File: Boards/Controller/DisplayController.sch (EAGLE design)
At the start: 47 parts, among them J1 USB0001LF, J100 38K8067, J3 AVR_SPI_PRG_62X3_LOCK, Q1 BSS138, U1 MCP1703CB, U100 MCP73831, U101 MAX1797, U2 FT232RQ, U3 ATMEGA328P-MU, U5 MAX1704X, X2 CRYSTAL7A-20.000MAAJ-T

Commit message: Added more xref labels to connections
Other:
- moved on the sheet: J100
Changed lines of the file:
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@@
 <setting verticaltext="up"/>
 </settings>
-<grid distance="0.1" unitdist="inch" unit="inch" style="lines" multiple="1" display="no" altdistance="0.01" altunitdist="inch" altunit="inch"/>
+<grid distance="0.1" unitdist="inch" unit="inch" style="lines" multiple="1" display="no" altdistance="0.05" altunitdist="inch" altunit="inch"/>
 <layers>
 <layer number="1" name="Top" color="4" fill="1" visible="no" active="no"/>
@@
 <part name="P+9" library="supply1" deviceset="VCC" device=""/>
 <part name="P+10" library="supply1" deviceset="VCC" device=""/>
+<part name="GND21" library="SparkFun" deviceset="GND" device=""/>
+<part name="GND27" library="SparkFun" deviceset="GND" device=""/>
+<part name="GND28" library="SparkFun" deviceset="GND" device=""/>
 </parts>
 <sheets>
@@
 <instance part="RN2" gate="A" x="109.22" y="157.48" rot="R270"/>
 <instance part="J2" gate="G$1" x="203.2" y="68.58"/>
-<instance part="J100" gate="G$1" x="160.02" y="93.98"/>
-<instance part="GND20" gate="1" x="172.72" y="86.36"/>
+<instance part="J100" gate="G$1" x="203.2" y="127"/>
+<instance part="GND20" gate="1" x="215.9" y="119.38"/>
 <instance part="J3" gate="G$1" x="200.66" y="93.98" smashed="yes">
 <attribute name="NAME" x="196.342" y="99.822" size="1.778" layer="95"/>
@@
 <instance part="RN1" gate="C" x="83.82" y="55.88"/>
 <instance part="R7" gate="G$1" x="22.86" y="134.62" rot="R180"/>
+<instance part="GND21" gate="1" x="213.36" y="88.9"/>
+<instance part="GND27" gate="1" x="220.98" y="76.2" rot="R90"/>
+<instance part="GND28" gate="1" x="185.42" y="66.04"/>
 </instances>
 <busses>
@@
 </segment>
 <segment>
-<wire x1="195.58" y1="68.58" x2="190.5" y2="68.58" width="0.1524" layer="91"/>
-<label x="190.5" y="68.58" size="1.778" layer="95"/>
+<wire x1="195.58" y1="68.58" x2="185.42" y2="68.58" width="0.1524" layer="91"/>
 <pinref part="J2" gate="G$1" pin="8"/>
+<pinref part="GND28" gate="1" pin="GND"/>
 </segment>
 <segment>
@@
 <wire x1="215.9" y1="76.2" x2="218.44" y2="76.2" width="0.1524" layer="91"/>
 <junction x="215.9" y="76.2"/>
-<label x="218.44" y="76.2" size="1.778" layer="95"/>
 <pinref part="J2" gate="G$1" pin="11"/>
 <pinref part="J2" gate="G$1" pin="13"/>
 <pinref part="J2" gate="G$1" pin="15"/>
-</segment>
-<segment>
-<wire x1="210.82" y1="91.44" x2="215.9" y2="91.44" width="0.1524" layer="91"/>
-<label x="215.9" y="91.44" size="1.778" layer="95"/>
+<pinref part="GND27" gate="1" pin="GND"/>
+</segment>
+<segment>
+<wire x1="210.82" y1="91.44" x2="213.36" y2="91.44" width="0.1524" layer="91"/>
+<wire x1="213.36" y1="91.44" x2="213.36" y2="90.17" width="0.1524" layer="91"/>
 <pinref part="J3" gate="G$1" pin="6"/>
-</segment>
-<segment>
-<wire x1="172.72" y1="93.98" x2="167.64" y2="93.98" width="0.1524" layer="91"/>
-<wire x1="172.72" y1="88.9" x2="172.72" y2="93.98" width="0.1524" layer="91"/>
+<pinref part="GND21" gate="1" pin="GND"/>
+<wire x1="213.36" y1="91.44" x2="213.36" y2="90.17" width="0.1524" layer="91"/>
+</segment>
+<segment>
+<wire x1="215.9" y1="127" x2="210.82" y2="127" width="0.1524" layer="91"/>
+<wire x1="215.9" y1="121.92" x2="215.9" y2="127" width="0.1524" layer="91"/>
 <pinref part="J100" gate="G$1" pin="1"/>
 <pinref part="GND20" gate="1" pin="GND"/>
@@
 </segment>
 <segment>
-<wire x1="193.04" y1="91.44" x2="187.96" y2="91.44" width="0.1524" layer="91"/>
-<label x="187.96" y="91.44" size="1.778" layer="95"/>
+<wire x1="193.04" y1="91.44" x2="190.5" y2="91.44" width="0.1524" layer="91"/>
+<wire x1="190.5" y1="91.44" x2="190.5" y2="90.17" width="0.1524" layer="91"/>
+<wire x1="190.5" y1="90.17" x2="187.96" y2="90.17" width="0.1524" layer="91"/>
 <pinref part="J3" gate="G$1" pin="5"/>
+<label x="187.96" y="90.17" size="1.778" layer="95" rot="R180" xref="yes"/>
 </segment>
 </net>
@@
 <segment>
 <pinref part="J2" gate="G$1" pin="7"/>
-<wire x1="210.82" y1="68.58" x2="215.9" y2="68.58" width="0.1524" layer="91"/>
-<label x="215.9" y="68.58" size="1.778" layer="95"/>
+<wire x1="210.82" y1="68.58" x2="213.36" y2="68.58" width="0.1524" layer="91"/>
+<wire x1="213.36" y1="68.58" x2="213.36" y2="69.85" width="0.1524" layer="91"/>
+<wire x1="213.36" y1="69.85" x2="215.9" y2="69.85" width="0.1524" layer="91"/>
+<label x="215.9" y="69.85" size="1.778" layer="95" xref="yes"/>
 </segment>
 </net>
 <net name="MISO" class="0">
 <segment>
-<wire x1="193.04" y1="96.52" x2="187.96" y2="96.52" width="0.1524" layer="91"/>
-<label x="187.96" y="96.52" size="1.778" layer="95"/>
+<wire x1="193.04" y1="96.52" x2="190.5" y2="96.52" width="0.1524" layer="91"/>
+<wire x1="190.5" y1="96.52" x2="190.5" y2="97.79" width="0.1524" layer="91"/>
+<wire x1="190.5" y1="97.79" x2="187.96" y2="97.79" width="0.1524" layer="91"/>
 <pinref part="J3" gate="G$1" pin="1"/>
+<label x="187.96" y="97.79" size="1.778" layer="95" rot="R180" xref="yes"/>
 </segment>
 <segment>
 <pinref part="J2" gate="G$1" pin="1"/>
 <wire x1="210.82" y1="60.96" x2="215.9" y2="60.96" width="0.1524" layer="91"/>
-<label x="215.9" y="60.96" size="1.778" layer="95"/>
+<label x="215.9" y="60.96" size="1.778" layer="95" xref="yes"/>
 </segment>
 </net>
@@
 <segment>
 <wire x1="210.82" y1="93.98" x2="215.9" y2="93.98" width="0.1524" layer="91"/>
-<label x="215.9" y="93.98" size="1.778" layer="95"/>
 <pinref part="J3" gate="G$1" pin="4"/>
+<label x="215.9" y="93.98" size="1.778" layer="95" xref="yes"/>
 </segment>
 <segment>
 <pinref part="J2" gate="G$1" pin="5"/>
 <wire x1="210.82" y1="66.04" x2="215.9" y2="66.04" width="0.1524" layer="91"/>
-<label x="215.9" y="66.04" size="1.778" layer="95"/>
+<label x="215.9" y="66.04" size="1.778" layer="95" xref="yes"/>
 </segment>
 </net>
@@
 <segment>
 <wire x1="193.04" y1="93.98" x2="187.96" y2="93.98" width="0.1524" layer="91"/>
-<label x="187.96" y="93.98" size="1.778" layer="95"/>
 <pinref part="J3" gate="G$1" pin="3"/>
+<label x="187.96" y="93.98" size="1.778" layer="95" rot="R180" xref="yes"/>
 </segment>
 <segment>
 <pinref part="J2" gate="G$1" pin="2"/>
 <wire x1="195.58" y1="60.96" x2="190.5" y2="60.96" width="0.1524" layer="91"/>
-<label x="190.5" y="60.96" size="1.778" layer="95"/>
+<label x="190.5" y="60.96" size="1.778" layer="95" rot="R180" xref="yes"/>
 </segment>
 </net>
 <net name="PACK+" class="0">
 <segment>
-<wire x1="167.64" y1="96.52" x2="172.72" y2="96.52" width="0.1524" layer="91"/>
-<label x="172.72" y="96.52" size="1.778" layer="95"/>
+<wire x1="210.82" y1="129.54" x2="215.9" y2="129.54" width="0.1524" layer="91"/>
 <pinref part="J100" gate="G$1" pin="2"/>
+<label x="215.9" y="129.54" size="1.778" layer="95" xref="yes"/>
 </segment>
 </net>
 <net name="N$11" class="0">
 <segment>
-<wire x1="210.82" y1="96.52" x2="215.9" y2="96.52" width="0.1524" layer="91"/>
-<label x="215.9" y="96.52" size="1.778" layer="95" font="vector"/>
+<wire x1="210.82" y1="96.52" x2="213.36" y2="96.52" width="0.1524" layer="91"/>
+<wire x1="213.36" y1="96.52" x2="213.36" y2="97.79" width="0.1524" layer="91"/>
+<wire x1="213.36" y1="97.79" x2="215.9" y2="97.79" width="0.1524" layer="91"/>
 <pinref part="J3" gate="G$1" pin="2"/>
+<label x="215.9" y="97.79" size="1.778" layer="95" xref="yes"/>
 </segment>
 </net>
@@
 <pinref part="U3" gate="A" pin="PC6"/>
 <wire x1="53.34" y1="86.36" x2="38.1" y2="86.36" width="0.1524" layer="91"/>
-<wire x1="38.1" y1="86.36" x2="38.1" y2="83.82" width="0.1524" layer="91"/>
-<wire x1="38.1" y1="83.82" x2="35.56" y2="83.82" width="0.1524" layer="91"/>
-<label x="35.56" y="83.82" size="1.778" layer="95" rot="R180" xref="yes"/>
+<wire x1="38.1" y1="86.36" x2="38.1" y2="85.09" width="0.1524" layer="91"/>
+<wire x1="38.1" y1="85.09" x2="35.56" y2="85.09" width="0.1524" layer="91"/>
+<label x="35.56" y="85.09" size="1.778" layer="95" rot="R180" xref="yes"/>
 </segment>
 </net>
@@
 <pinref part="U3" gate="A" pin="PC4"/>
 <wire x1="53.34" y1="91.44" x2="38.1" y2="91.44" width="0.1524" layer="91"/>
-<wire x1="38.1" y1="91.44" x2="38.1" y2="93.98" width="0.1524" layer="91"/>
-<wire x1="38.1" y1="93.98" x2="35.56" y2="93.98" width="0.1524" layer="91"/>
-<label x="35.56" y="93.98" size="1.778" layer="95" rot="R180" xref="yes"/>
+<wire x1="38.1" y1="91.44" x2="38.1" y2="92.71" width="0.1524" layer="91"/>
+<wire x1="38.1" y1="92.71" x2="35.56" y2="92.71" width="0.1524" layer="91"/>
+<label x="35.56" y="92.71" size="1.778" layer="95" rot="R180" xref="yes"/>
 </segment>
 <segment>
@@
 <wire x1="149.86" y1="96.52" x2="149.86" y2="101.6" width="0.1524" layer="91"/>
 <junction x="149.86" y="101.6"/>
-</segment>
-</net>
+<label x="147.32" y="101.6" size="1.778" layer="95" rot="R180" xref="yes"/>
+</segment>
+</net>

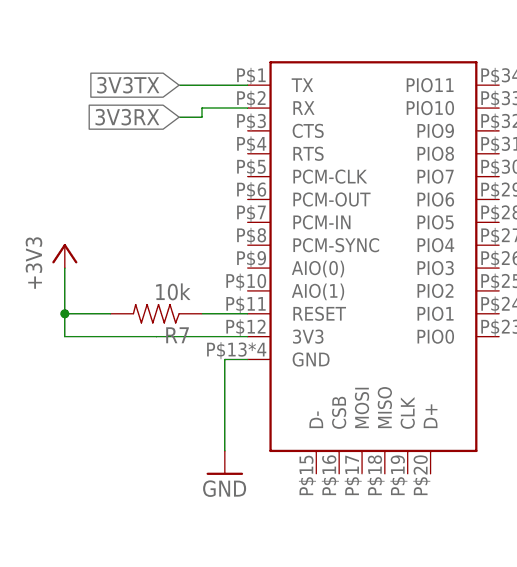
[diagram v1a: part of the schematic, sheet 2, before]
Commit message: connected bluetooth reset to microcontroller
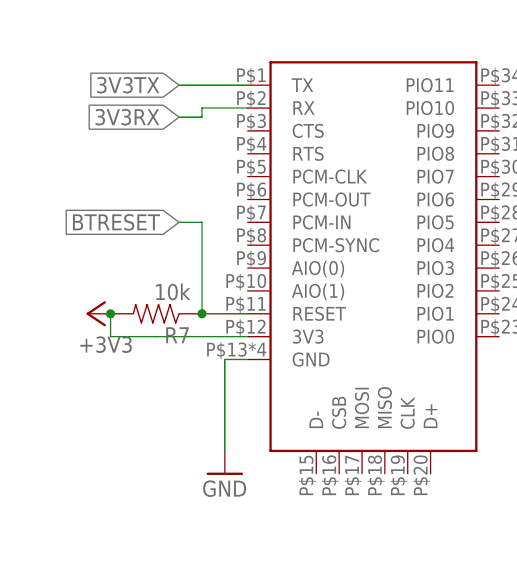
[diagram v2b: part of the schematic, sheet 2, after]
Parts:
- removed S1: TL1015AF160QG, MyParts:TL1015AF160QG
- added S3: SWITCH-MOMENTARY-2SMD, SparkFun:SWITCH-MOMENTARY-2SMD
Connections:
- net BTRESET: now also U3.PC0
- net GND: now also S3.1; no longer S1.P$1
- net RESET: now also S3.2; no longer S1.P$2
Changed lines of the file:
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@@
 <setting verticaltext="up"/>
 </settings>
-<grid distance="0.1" unitdist="inch" unit="inch" style="lines" multiple="1" display="no" altdistance="0.05" altunitdist="inch" altunit="inch"/>
+<grid distance="0.1" unitdist="inch" unit="inch" style="lines" multiple="1" display="no" altdistance="0.01" altunitdist="inch" altunit="inch"/>
 <layers>
 <layer number="1" name="Top" color="4" fill="1" visible="no" active="no"/>
@@
 <attribute name="OC_NEWARK" value="15M6872"/>
 </part>
-<part name="S1" library="MyParts" deviceset="TL1015" device="AF160QG"/>
 <part name="U5" library="SparkFun" deviceset="MAX1704X" device=""/>
 <part name="GND7" library="supply1" deviceset="GND" device=""/>
@@
 <part name="GND27" library="SparkFun" deviceset="GND" device=""/>
 <part name="GND28" library="SparkFun" deviceset="GND" device=""/>
+<part name="S3" library="SparkFun" deviceset="SWITCH-MOMENTARY-2" device="SMD"/>
 </parts>
 <sheets>
@@
 </instance>
 <instance part="GND8" gate="1" x="30.48" y="116.84"/>
-<instance part="+3V3" gate="G$1" x="12.7" y="142.24"/>
+<instance part="+3V3" gate="G$1" x="15.24" y="134.62" rot="R90"/>
 <instance part="+3V4" gate="G$1" x="88.9" y="167.64"/>
 <instance part="P+3" gate="1" x="109.22" y="172.72"/>
@@
 <pinref part="+3V3" gate="G$1" pin="+3V3"/>
 <wire x1="33.02" y1="132.08" x2="22.86" y2="132.08" width="0.1524" layer="91"/>
-<wire x1="22.86" y1="132.08" x2="12.7" y2="132.08" width="0.1524" layer="91"/>
-<wire x1="12.7" y1="132.08" x2="12.7" y2="134.62" width="0.1524" layer="91"/>
+<wire x1="22.86" y1="132.08" x2="17.78" y2="132.08" width="0.1524" layer="91"/>
+<wire x1="17.78" y1="132.08" x2="17.78" y2="134.62" width="0.1524" layer="91"/>
 <pinref part="R7" gate="G$1" pin="2"/>
-<wire x1="12.7" y1="134.62" x2="12.7" y2="139.7" width="0.1524" layer="91"/>
-<wire x1="17.78" y1="134.62" x2="12.7" y2="134.62" width="0.1524" layer="91"/>
-<junction x="12.7" y="134.62"/>
+<junction x="17.78" y="134.62"/>
 </segment>
 <segment>
@@
 <wire x1="27.94" y1="134.62" x2="33.02" y2="134.62" width="0.1524" layer="91"/>
 <pinref part="R7" gate="G$1" pin="1"/>
+<wire x1="27.94" y1="134.62" x2="27.94" y2="144.78" width="0.1524" layer="91"/>
+<wire x1="27.94" y1="144.78" x2="25.4" y2="144.78" width="0.1524" layer="91"/>
+<junction x="27.94" y="134.62"/>
+<label x="25.4" y="144.78" size="1.778" layer="95" rot="R180" xref="yes"/>
 </segment>
 </net>
@@
 <instance part="RN3" gate="B" x="104.14" y="127"/>
 <instance part="RN3" gate="C" x="104.14" y="121.92"/>
-<instance part="S1" gate="G$1" x="12.7" y="127" rot="R90"/>
 <instance part="U5" gate="G$1" x="187.96" y="99.06"/>
 <instance part="GND7" gate="1" x="172.72" y="88.9"/>
@@
 <instance part="P+9" gate="VCC" x="33.02" y="76.2"/>
 <instance part="P+10" gate="VCC" x="22.86" y="76.2"/>
+<instance part="S3" gate="G$1" x="12.7" y="121.92" rot="R90"/>
 </instances>
 <busses>
@@
 </segment>
 <segment>
-<wire x1="12.7" y1="119.38" x2="12.7" y2="116.84" width="0.1524" layer="91"/>
 <pinref part="GND14" gate="1" pin="GND"/>
-<pinref part="S1" gate="G$1" pin="P$1"/>
+<pinref part="S3" gate="G$1" pin="1"/>
 </segment>
 <segment>
@@
 <label x="17.78" y="132.08" size="1.778" layer="95" xref="yes"/>
 <pinref part="R101" gate="G$1" pin="1"/>
-<pinref part="S1" gate="G$1" pin="P$2"/>
-<wire x1="12.7" y1="132.08" x2="12.7" y2="129.54" width="0.1524" layer="91"/>
+<wire x1="12.7" y1="132.08" x2="12.7" y2="127" width="0.1524" layer="91"/>
 <wire x1="17.78" y1="132.08" x2="12.7" y2="132.08" width="0.1524" layer="91"/>
 <junction x="12.7" y="132.08"/>
+<pinref part="S3" gate="G$1" pin="2"/>
 </segment>
 <segment>
@@
 </segment>
 </net>
+<net name="BTRESET" class="0">
+<segment>
+<pinref part="U3" gate="A" pin="PC0"/>
+<wire x1="53.34" y1="101.6" x2="40.64" y2="101.6" width="0.1524" layer="91"/>
+<label x="40.64" y="101.6" size="1.778" layer="95" rot="R180" xref="yes"/>
+</segment>
+</net>

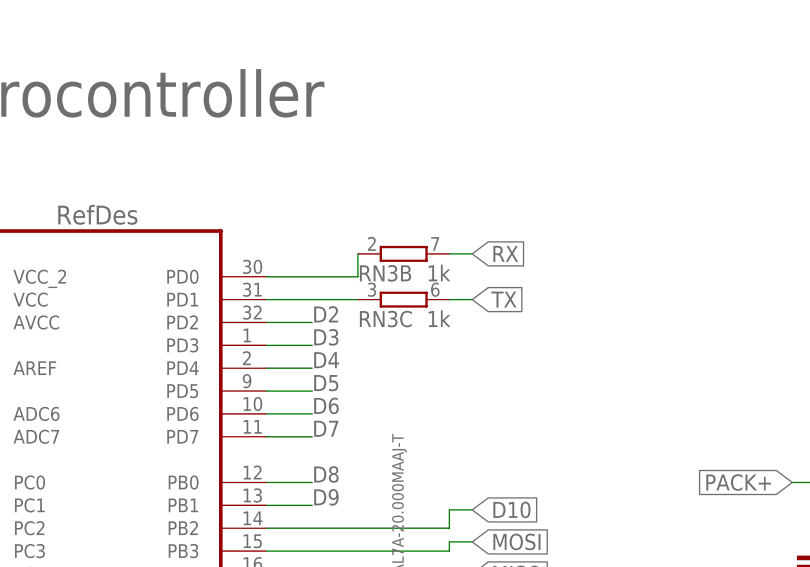
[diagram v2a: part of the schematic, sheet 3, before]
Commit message: removed 1K resistor from TX + RX between ATMega328p and FT232RQ, not needed as nothing else is connected to these pins.
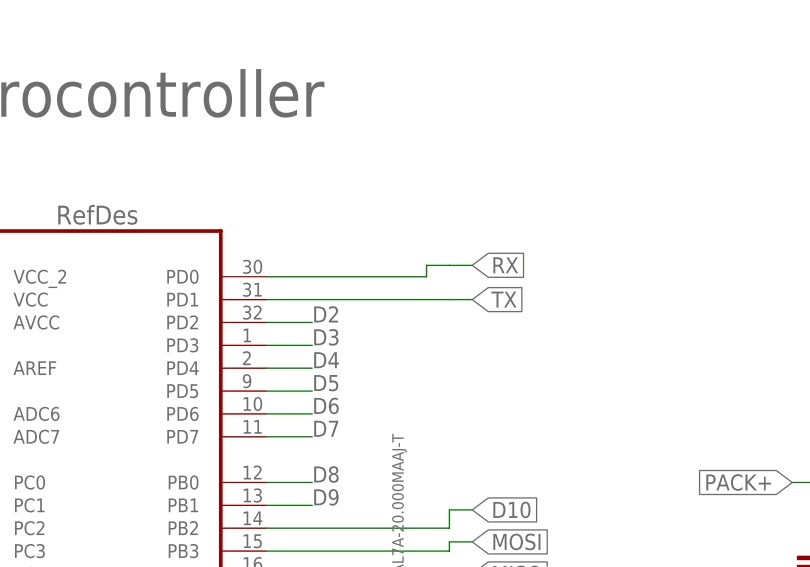
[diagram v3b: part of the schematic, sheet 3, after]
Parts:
- removed RN3: 1k, resistor-dil:4R-NEXB38V
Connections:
- removed net N$13: RN3C.1, U3.PD1
- removed net N$15: RN3B.1, U3.PD0
- net RX: now also U3.PD0; no longer RN3B.2
- net TX: now also U3.PD1; no longer RN3C.2
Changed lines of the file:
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@@
 <part name="GND6" library="SparkFun" deviceset="GND" device=""/>
 <part name="U2" library="SparkFun" deviceset="FT232RQ" device=""/>
-<part name="RN3" library="resistor-dil" deviceset="4R-N" device="EXB38V" value="1k">
-<attribute name="OC_NEWARK" value="15M6870"/>
-</part>
 <part name="J1" library="MyParts" deviceset="USB" device="0001LF">
 <attribute name="NEWARK_PN" value="82R7424"/>
@@
 <instance part="C7" gate="G$1" x="106.68" y="73.66" rot="MR270"/>
 <instance part="U3" gate="A" x="71.12" y="101.6"/>
-<instance part="RN3" gate="B" x="104.14" y="127"/>
-<instance part="RN3" gate="C" x="104.14" y="121.92"/>
 <instance part="U5" gate="G$1" x="187.96" y="99.06"/>
 <instance part="GND7" gate="1" x="172.72" y="88.9"/>
@@
 <net name="RX" class="0">
 <segment>
-<pinref part="RN3" gate="B" pin="2"/>
-<wire x1="109.22" y1="127" x2="111.76" y2="127" width="0.1524" layer="91"/>
-<label x="111.76" y="127" size="1.778" layer="95" xref="yes"/>
+<wire x1="109.22" y1="125.73" x2="111.76" y2="125.73" width="0.1524" layer="91"/>
+<label x="111.76" y="125.73" size="1.778" layer="95" xref="yes"/>
+<pinref part="U3" gate="A" pin="PD0"/>
+<wire x1="88.9" y1="124.46" x2="106.68" y2="124.46" width="0.1524" layer="91"/>
+<wire x1="106.68" y1="124.46" x2="106.68" y2="125.73" width="0.1524" layer="91"/>
+<wire x1="109.22" y1="125.73" x2="106.68" y2="125.73" width="0.1524" layer="91"/>
 </segment>
 </net>
 <net name="TX" class="0">
 <segment>
-<pinref part="RN3" gate="C" pin="2"/>
 <wire x1="109.22" y1="121.92" x2="111.76" y2="121.92" width="0.1524" layer="91"/>
 <label x="111.76" y="121.92" size="1.778" layer="95" xref="yes"/>
-</segment>
-</net>
-<net name="N$13" class="0">
-<segment>
 <pinref part="U3" gate="A" pin="PD1"/>
-<pinref part="RN3" gate="C" pin="1"/>
 <wire x1="88.9" y1="121.92" x2="99.06" y2="121.92" width="0.1524" layer="91"/>
-</segment>
-</net>
-<net name="N$15" class="0">
-<segment>
-<pinref part="U3" gate="A" pin="PD0"/>
-<pinref part="RN3" gate="B" pin="1"/>
-<wire x1="88.9" y1="124.46" x2="99.06" y2="124.46" width="0.1524" layer="91"/>
-<wire x1="99.06" y1="124.46" x2="99.06" y2="127" width="0.1524" layer="91"/>
-</segment>
-</net>
+<wire x1="109.22" y1="121.92" x2="99.06" y2="121.92" width="0.1524" layer="91"/>
+</segment>
+</net>

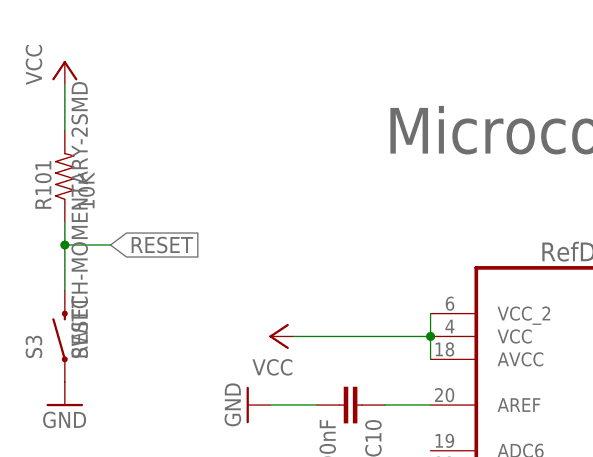
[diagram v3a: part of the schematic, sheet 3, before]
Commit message: Added Switching diode to reset line on atmega328 (per arduino forums/Uno R3 design)
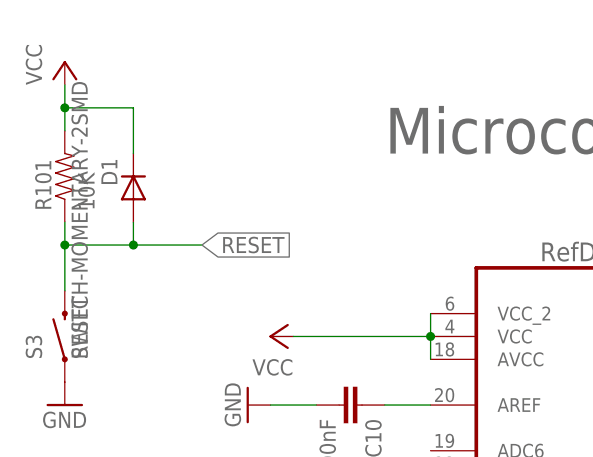
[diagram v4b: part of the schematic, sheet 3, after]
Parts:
- added D1: (no value), MyParts:LEDSML1206
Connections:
- net RESET: now also D1.A
- net VCC: now also D1.C
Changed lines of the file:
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@@
 <part name="GND28" library="SparkFun" deviceset="GND" device=""/>
 <part name="S3" library="SparkFun" deviceset="SWITCH-MOMENTARY-2" device="SMD"/>
+<part name="D1" library="MyParts" deviceset="LED" device="SML1206">
+<attribute name="NEWARK_PN" value="09J8040"/>
+</part>
 </parts>
 <sheets>
@@
 <instance part="P+10" gate="VCC" x="22.86" y="76.2"/>
 <instance part="S3" gate="G$1" x="12.7" y="121.92" rot="R90"/>
+<instance part="D1" gate="G$1" x="20.32" y="137.16" rot="R180">
+<attribute name="NEWARK_PN" x="20.32" y="137.16" size="1.778" layer="96" rot="R180" display="off"/>
+</instance>
 </instances>
 <busses>
@@
 </segment>
 <segment>
-<wire x1="12.7" y1="149.86" x2="12.7" y2="144.78" width="0.1524" layer="91"/>
+<wire x1="12.7" y1="149.86" x2="12.7" y2="147.32" width="0.1524" layer="91"/>
 <pinref part="R101" gate="G$1" pin="2"/>
 <pinref part="P+6" gate="VCC" pin="VCC"/>
+<pinref part="D1" gate="G$1" pin="C"/>
+<wire x1="12.7" y1="147.32" x2="12.7" y2="144.78" width="0.1524" layer="91"/>
+<wire x1="20.32" y1="142.24" x2="20.32" y2="147.32" width="0.1524" layer="91"/>
+<wire x1="20.32" y1="147.32" x2="12.7" y2="147.32" width="0.1524" layer="91"/>
+<junction x="12.7" y="147.32"/>
 </segment>
 <segment>
@@
 <segment>
 <wire x1="12.7" y1="134.62" x2="12.7" y2="132.08" width="0.1524" layer="91"/>
-<label x="17.78" y="132.08" size="1.778" layer="95" xref="yes"/>
+<label x="27.94" y="132.08" size="1.778" layer="95" xref="yes"/>
 <pinref part="R101" gate="G$1" pin="1"/>
 <wire x1="12.7" y1="132.08" x2="12.7" y2="127" width="0.1524" layer="91"/>
-<wire x1="17.78" y1="132.08" x2="12.7" y2="132.08" width="0.1524" layer="91"/>
+<wire x1="27.94" y1="132.08" x2="20.32" y2="132.08" width="0.1524" layer="91"/>
 <junction x="12.7" y="132.08"/>
 <pinref part="S3" gate="G$1" pin="2"/>
-</segment>
-<segment>
+<pinref part="D1" gate="G$1" pin="A"/>
+<wire x1="20.32" y1="132.08" x2="12.7" y2="132.08" width="0.1524" layer="91"/>
+<wire x1="20.32" y1="134.62" x2="20.32" y2="132.08" width="0.1524" layer="91"/>
+<junction x="20.32" y="132.08"/>
+</segment>
+<segment>
